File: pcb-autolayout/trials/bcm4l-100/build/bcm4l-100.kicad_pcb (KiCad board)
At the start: 4 copper layers, 80 x 60 mm, 120 parts, among them J1 MicroFit 2x4, J2 MicroFit 2x6, J3 SWD, Q1 SQD40P06 (P-MOS), Q11 AO3401A, Q12 MMBT3904, Q13 AO3401A, Q14 MMBT3904, Q15 AO3401A, Q16 MMBT3904, Q17 AO3401A, Q18 MMBT3904, SW1 RESET, U1 TPS54202, U2 AMS1117-3.3, U3 TJA1051T/3, U4 TJA1021T/20, U5 STM32F103C8T6, Y1 8MHz

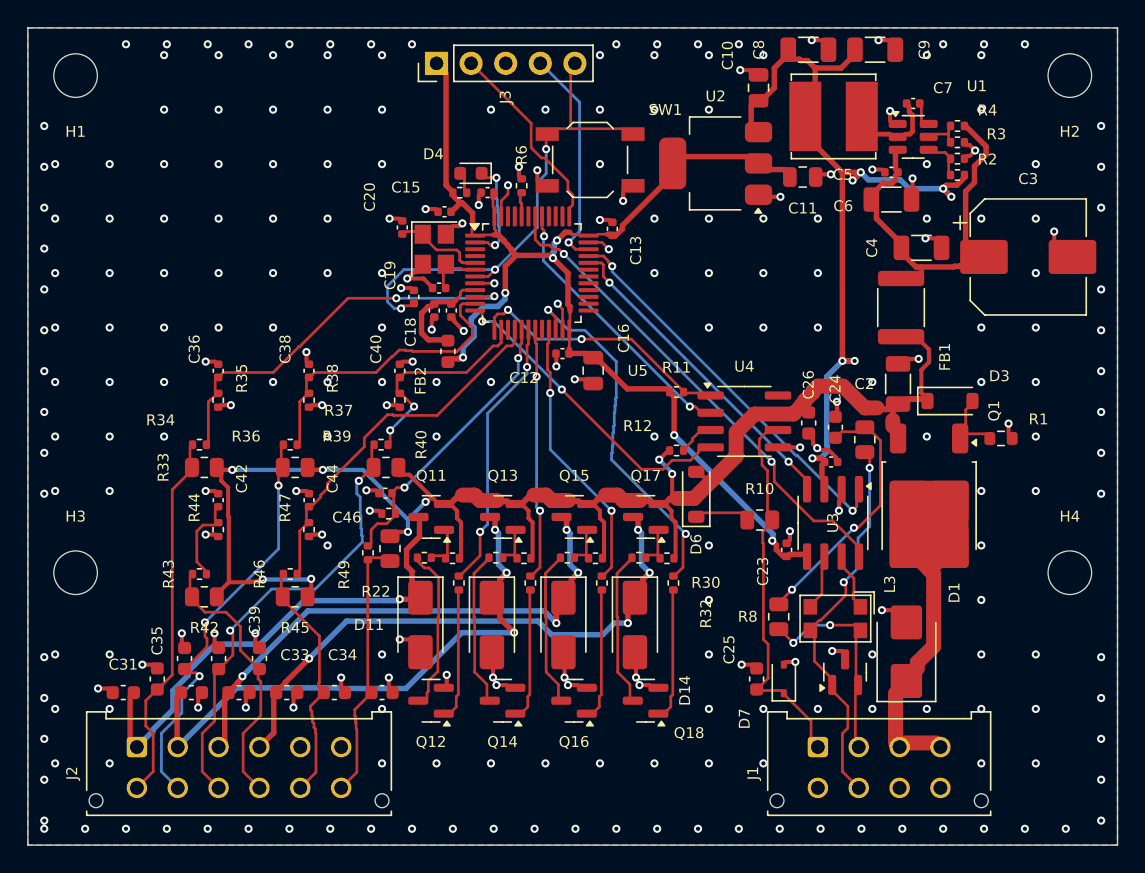
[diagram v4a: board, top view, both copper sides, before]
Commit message: C0: toàn trình chạy trên KiCad 9.0.8, tất định; vá cổng release; --reuse-routes
- kicad_board: GetDefaultNetclass() (KiCad 9) / m_DefaultNetClass (KiCad 7)
- release.py: mặc định checks.json cạnh board, thiếu -> từ chối; board khác hash.txt -> từ chối
- run.py --reuse-routes: dùng lại routes.json khi khoá đầu vào khớp (đối chứng cùng hash)
- setup-kicad9.sh: thêm librsvg2-bin
- trial bcm4l-100 build lại trên KiCad 9: 13/16 rule, DRC 0, hash cdfd7b4d4849eec8 (2 lượt trùng)
- REPORT vòng 5, PLAN-v2 C0, skill route/release/autolayout

Co-Authored-By: Claude Opus 5.5 <noreply@anthropic.com>
Claude-Session: https://claude.ai/code/session_012jwodCpQFB8wopi3P3TnUz
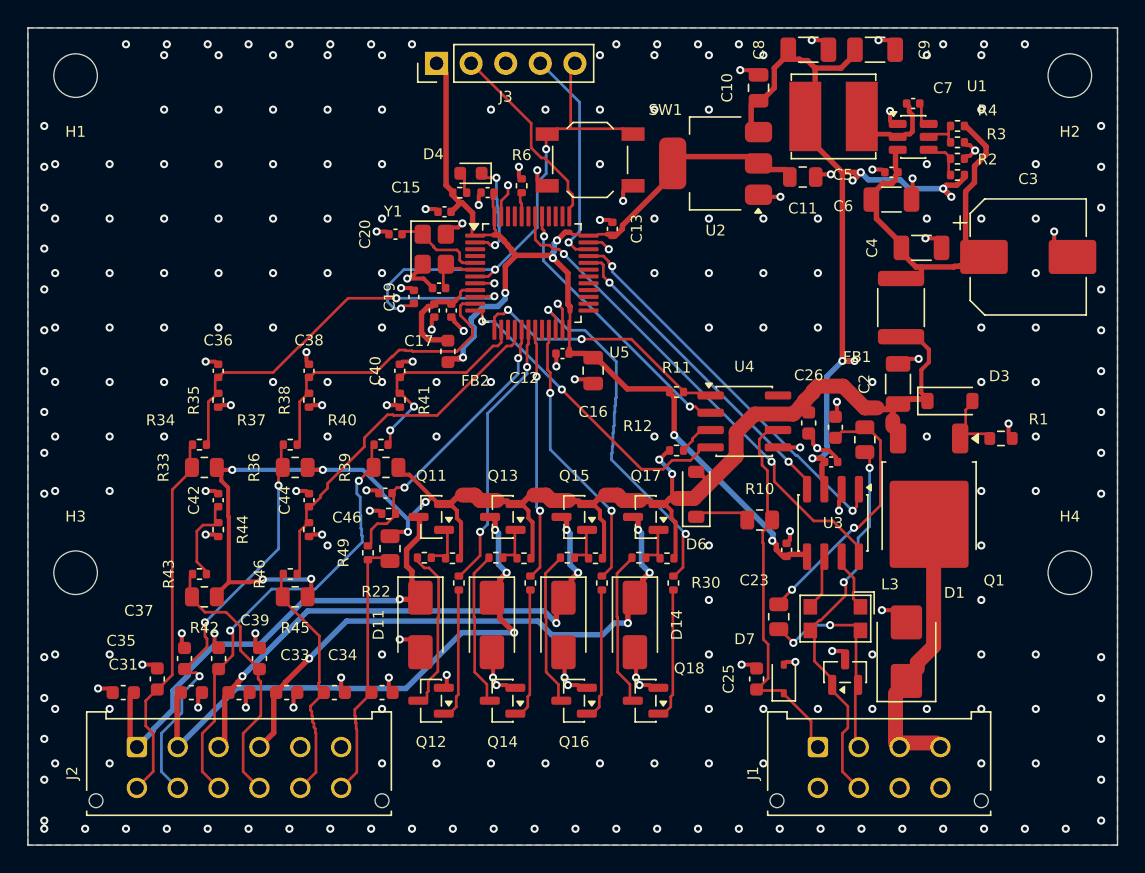
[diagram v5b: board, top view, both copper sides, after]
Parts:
- removed the C10 at (153.6, 64.4)
- removed the C20 at (127.5, 74.7)
- removed the C21 at (130.2, 79.1)
- removed the C25 at (153.5, 107.8)
- removed the C37 at (111.5, 106.3)
- removed the C5 at (163.4, 72.6)
- removed the C6 at (163.4, 70.6)
- removed the D12 at (134.1, 103.8)
- removed the D4 at (132.5, 70.7)
- removed the U3 at (159.1, 96.3)
- added C15: 100n, Capacitor_SMD:C_0402_1005Metric, F.Cu at (130.6, 73.5)
- added C19: 100n, Capacitor_SMD:C_0402_1005Metric, F.Cu at (128.3, 79.8)
- added C22: 100n, Capacitor_SMD:C_0402_1005Metric, F.Cu at (159.0, 91.9)
- added C31: 10n 50V, Capacitor_SMD:C_0603_1608Metric, F.Cu at (107.0, 108.8)
- added C32: 10n 50V, Capacitor_SMD:C_0603_1608Metric, F.Cu at (112.0, 108.8)
- added C45: 10n 50V, Capacitor_SMD:C_0603_1608Metric, F.Cu at (126.0, 108.8)
- added C46: 10n, Capacitor_SMD:C_0402_1005Metric, F.Cu at (126.2, 94.2)
- added D6: BAS21, Diode_SMD:D_SOD-123, F.Cu at (149.1, 94.2)
- added H1: M3, MountingHole:MountingHole_3.2mm_M3, F.Cu at (103.5, 63.5)
- added J1: MicroFit 2x4, Connector_Molex:Molex_Micro-Fit_3.0_43045-0812_2x04_P3.00mm_Vertical, F.Cu at (158.0, 112.8)
- C10: renamed from C41; value 10n 50V -> 10u; footprint Capacitor_SMD:C_0603_1608Metric -> Capacitor_SMD:C_0805_2012Metric
- C20: renamed from C46; value 10n -> 20p
- C21: renamed from C19; value 100n -> 20p
- C25: renamed from C32; value 10n 50V -> 1n 50V
- C37: renamed from C22; value 100n -> 10n 50V; footprint Capacitor_SMD:C_0402_1005Metric -> Capacitor_SMD:C_0603_1608Metric
- C5: renamed from C45; value 10n 50V -> 10u 50V; footprint Capacitor_SMD:C_0603_1608Metric -> Capacitor_SMD:C_1206_3216Metric
- C6: renamed from C12; value 100n -> 100n 50V
- D12: renamed from J1; value MicroFit 2x4 -> SS14; footprint Connector_Molex:Molex_Micro-Fit_3.0_43045-0812_2x04_P3.00mm_Vertical -> Diode_SMD:D_SMA
- D4: renamed from D6; value BAS21 -> LED; footprint Diode_SMD:D_SOD-123 -> LED_SMD:LED_0603_1608Metric
- U3: renamed from H1; value M3 -> TJA1051T/3; footprint MountingHole:MountingHole_3.2mm_M3 -> Package_SO:SOIC-8_3.9x4.9mm_P1.27mm
- moved U3 64.6 mm to (159.1, 96.3), turned to -90 degrees
- moved C10 55.7 mm to (153.6, 64.4)
- moved C5 52.0 mm to (163.4, 72.6)
- moved C37 49.6 mm to (111.5, 106.3), turned to 90 degrees
- moved C25 41.5 mm to (153.5, 107.8), turned to 90 degrees
- moved D4 28.8 mm to (132.5, 70.7), turned to 180 degrees
- moved C6 27.6 mm to (163.4, 70.6)
- moved D12 25.6 mm to (134.1, 103.8), turned to -90 degrees
- moved C20 19.0 mm to (127.0, 75.2)
- moved C12 13.5 mm to (139.2, 83.9)
- moved C41 10.3 mm to (117.0, 106.3), turned to 90 degrees
- moved C21 1.96 mm to (130.2, 79.1), turned to 180 degrees
- renumbered C15 to C12, C31 to C41
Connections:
- C10 pad 1: IN4 -> +5V
- C20 pad 1: IN6_M -> OSC_IN
- C21 pad 1: NRST -> OSC_OUT
- C25 pad 1: OUT2 -> LIN
- C37 pad 1: +5V -> IN2
- C41 pad 1: OUT1 -> IN4
- C5 pad 1: IN6 -> VBAT_F
- C6 pad 1: +3V3 -> VBAT_F
- D12 pad 1: LIN -> OUT2
- D12 pad 2: CANH -> GND
- D4 pad 1: LIN_PU -> LED_K
- D4 pad 2: VBAT_P -> LED_A
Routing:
- net VBAT_IN: track 15.6 -> 14.8 mm
- net GND: track 61.5 -> 61.7 mm, vias 265 -> 266

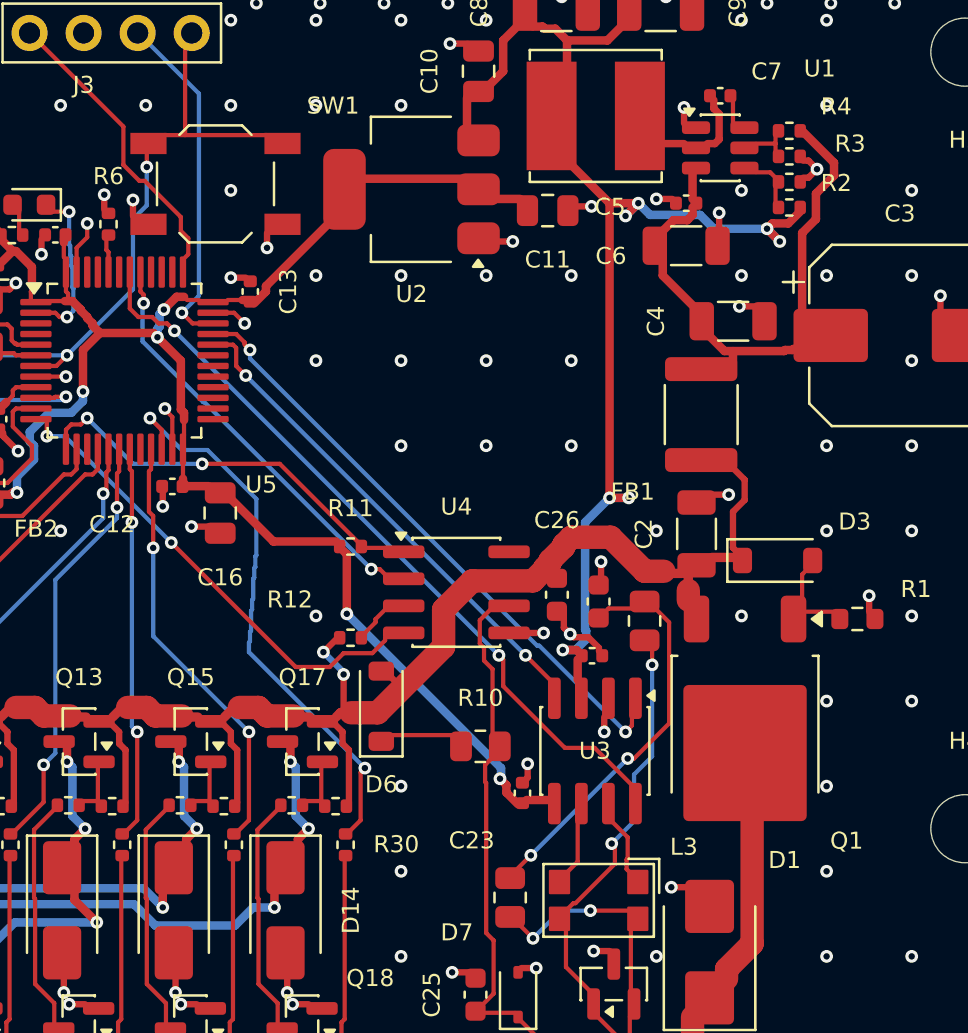
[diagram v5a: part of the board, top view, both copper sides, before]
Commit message: bcm4l-100: build lại sau sửa lowcur FB1 (KiCad 9); kiểm skill SKIP verify/release khi toolchain khác
- 13/16 rule, DRC 0, 886 đoạn, 343 via, hash 8610206f44f28438; nhánh FB1 1.10 mm
- run_skills: 8/8 PASS trên KiCad 9; KiCad 7 SKIP có lý do (board mốc định dạng KiCad 9)
- REPORT vòng 6

Co-Authored-By: Claude Opus 5.5 <noreply@anthropic.com>
Claude-Session: https://claude.ai/code/session_012jwodCpQFB8wopi3P3TnUz
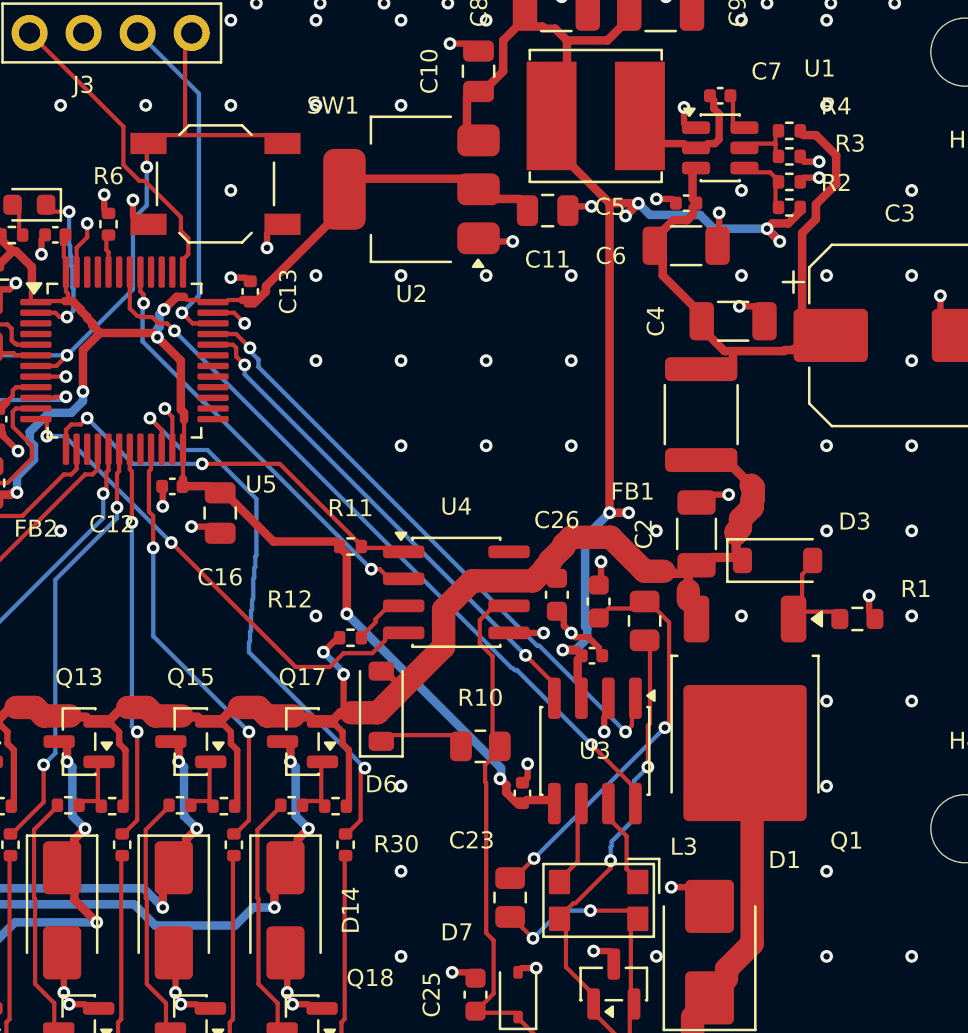
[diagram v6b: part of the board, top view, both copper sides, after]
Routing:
- net CAN_S: track 34.7 -> 33.9 mm
- net GND: track 61.7 -> 61.5 mm, vias 266 -> 267

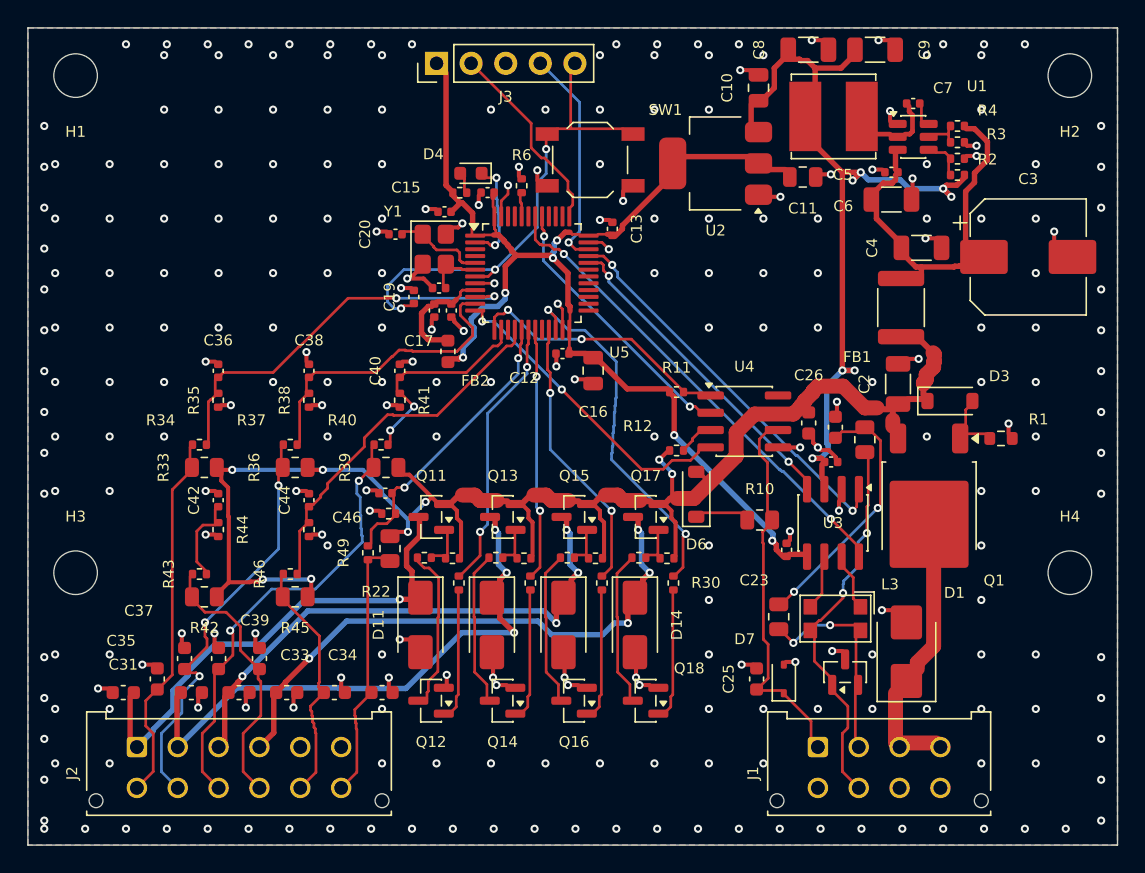
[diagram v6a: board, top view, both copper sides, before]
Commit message: A1: router 6x nhanh hơn (931->150 s), 15/16 rule
- router_core: trạng thái via vào heap thiếu heuristic (f=g) -> A* thành Dijkstra; sửa thành g+h.
  Chân hở U5.15 ('thiếu dung lượng') biến mất — chẩn đoán T34 cũ sai
- PathFinder dừng khi 5 vòng không lập kỷ lục (điều kiện cũ không bao giờ kích hoạt)
- net >= 1 A buộc đổi lớp: chọn vị trí đủ chỗ cụm via + giữ chỗ trong dấu chân -> PWR-005 đạt
- reinforce: 16 hướng x 8 khoảng; tools/prof_route.py, tools/diag_via.py
- run_skills: ca âm release tự dựng khi board sạch
- trial: 15/16, DRC 0, hash 9c30d6f3daadd940

Co-Authored-By: Claude Opus 5.5 <noreply@anthropic.com>
Claude-Session: https://claude.ai/code/session_012jwodCpQFB8wopi3P3TnUz
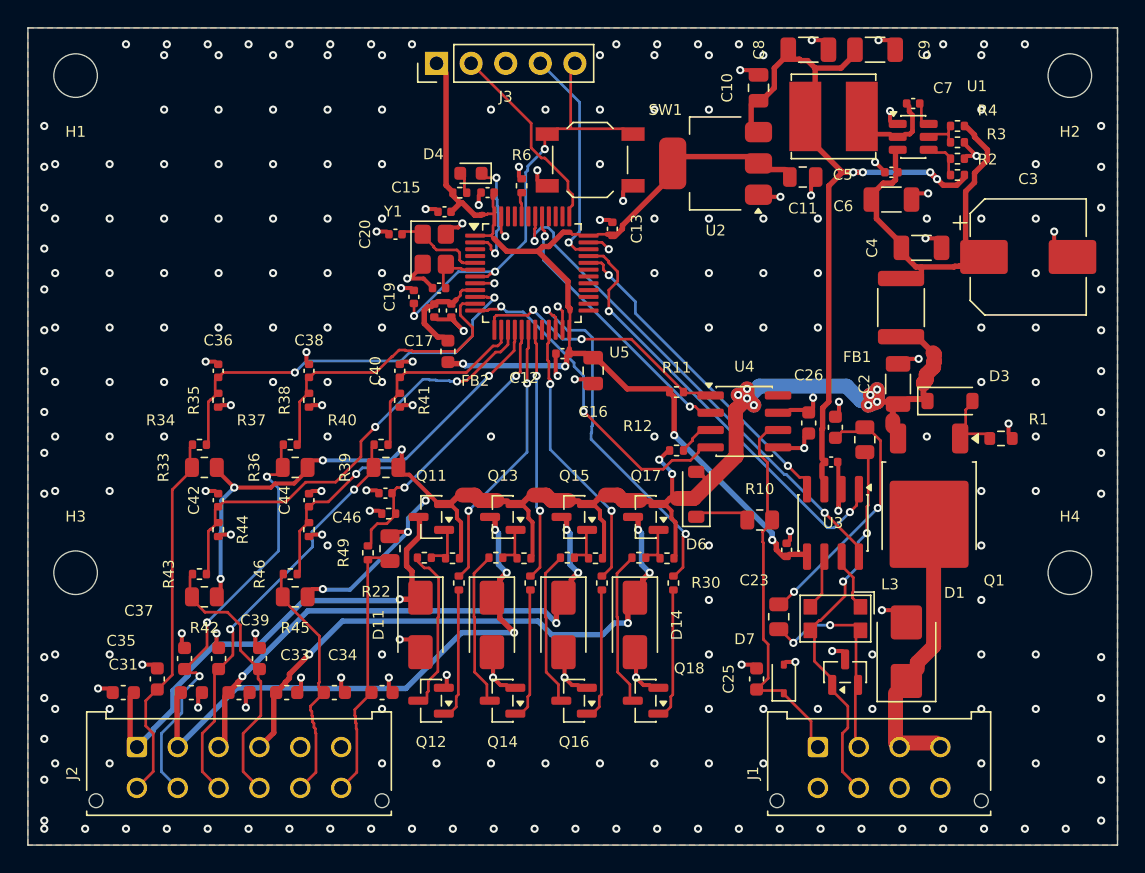
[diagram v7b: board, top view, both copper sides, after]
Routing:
- net IN4_M: track 5.58 -> 31.6 mm, vias 0 -> 2
- net VBAT_P: track 101.9 -> 112.9 mm, vias 8 -> 18
- net GND: track 61.5 -> 66.4 mm, vias 267 -> 258
- net +5V: track 52.1 -> 48.1 mm, vias 7 -> 4
- net NRST: track 33.0 -> 29.6 mm
- net CAN_TX: track 27.6 -> 30.9 mm
- net IN3: track 31.0 -> 28.5 mm
- net CAN_S: track 33.9 -> 35.6 mm
- net +3V3: track 76.0 -> 74.3 mm, vias 6 -> 4
- net LIN_TX: track 21.8 -> 23.2 mm
- net LED_K: track 6.84 -> 7.83 mm
- net IN2: track 28.1 -> 29.1 mm
- net IN3_M: track 13.8 -> 12.9 mm, vias 2 -> 0
- net +3V3A: track 6.41 -> 5.64 mm
- net IN1_M: track 27.7 -> 28.4 mm
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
